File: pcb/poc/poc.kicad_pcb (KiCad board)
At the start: 2 copper layers, 100 x 100 mm, 59 parts, among them J1 USB_B_Mini, J2 Right, J3 Left, J4 AVR-ISP-6, J5 Conn_02x10_Odd_Even, J6 Conn_02x06_Odd_Even, SW1 SW_Push, SW10 SW_Push_45deg, SW11 SW_Push_45deg, SW2 SW_Push_45deg, SW3 SW_Push_45deg, SW4 SW_Push_45deg, SW5 SW_Push_45deg, SW6 SW_Push_45deg, SW7 SW_Push_45deg, SW8 SW_Push_45deg, SW9 SW_Push_45deg, U1 ATmega32U4-AU, U2 MCP23018_SO, Y1 16MHz

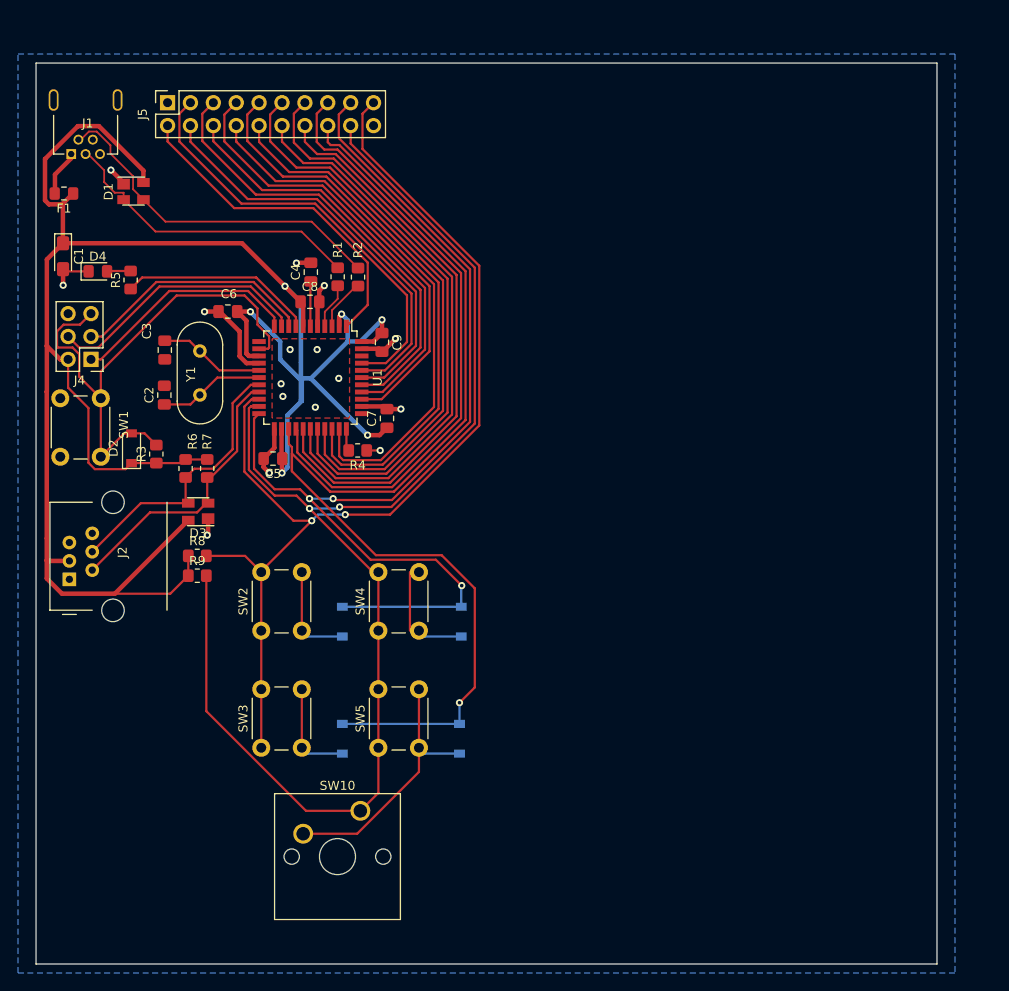
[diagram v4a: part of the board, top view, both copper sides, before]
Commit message: pcb: poc: i2c breakout and crystal ground
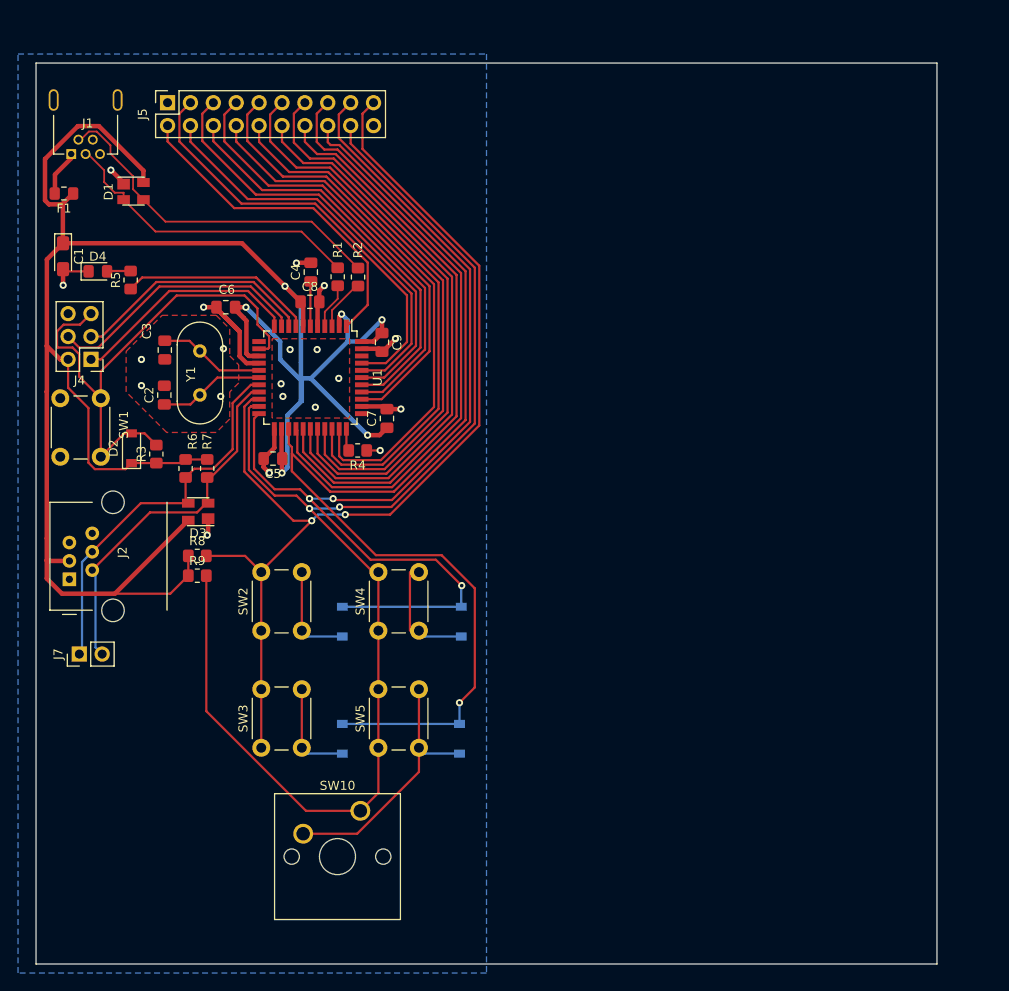
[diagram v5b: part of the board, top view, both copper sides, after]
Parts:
- added J7: Conn_01x02, Connector_PinHeader_2.54mm:PinHeader_1x02_P2.54mm_Vertical, F.Cu at (74.8, 120.6)
- moved C6 0.53 mm to (91.1, 82.1)
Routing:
- net /SCL: track 31.3 -> 43.2 mm
- net /SDA: track 31.4 -> 41.2 mm
- net GND: track 41.3 -> 45.0 mm, vias 16 -> 20
- net +5V: track 240.9 -> 243.1 mm

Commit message: pcb: poc: MCP side layout
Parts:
- added C10: 100n, Capacitor_SMD:C_0805_2012Metric_Pad1.18x1.45mm_HandSolder, F.Cu at (145.8, 75.5)
- D11, D12, D13, D14: moved to B.Cu
- moved J6 233.5 mm to (133.2, 102.5), turned to 90 degrees
- moved D14 222.5 mm to (165.0, 130.0), turned to 270 degrees
- moved SW8 214.9 mm to (156.0, 118.0), turned to 90 degrees
- moved D12 212.9 mm to (152.0, 130.0), turned to 270 degrees
- moved SW6 208.1 mm to (143.0, 118.0), turned to 90 degrees
- moved SW11 205.3 mm to (154.0, 138.0)
- moved SW9 201.1 mm to (156.0, 131.0), turned to 90 degrees
- moved U2 198.1 mm to (141.1, 67.2), turned to 90 degrees
- moved R13 197.6 mm to (135.2, 76.4), turned to 270 degrees
- moved SW7 194.5 mm to (143.0, 131.0), turned to 90 degrees
- moved R12 166.6 mm to (151.9, 63.5), turned to 90 degrees
- moved D11 160.4 mm to (152.0, 117.0), turned to 270 degrees
- moved D13 158.1 mm to (165.0, 117.0), turned to 270 degrees
- moved R10 156.3 mm to (150.5, 57.3), turned to 180 degrees
- moved R15 154.5 mm to (145.8, 59.7), turned to 180 degrees
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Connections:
- D5 pad 2: /SCL1 -> /SDA1
- D5 pad 3: /SDA1 -> /SCL1
- SW11 pad 2: Net-(D13-Pad2) -> Net-(D14-Pad2)
- U2 pad 20: /COL3 -> /COL4
- U2 pad 21: /COL4 -> /COL3
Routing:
- net /ROW3: track 0.00 -> 79.3 mm, vias 0 -> 1
- net /ROW2: track 0.00 -> 65.6 mm, vias 0 -> 1
- net +5VP: track 0.00 -> 60.9 mm
- net /COL4: track 0.00 -> 27.3 mm
- net Net-(D14-Pad2): track 0.00 -> 25.4 mm
- net /SCL1: track 0.00 -> 21.1 mm
- net /COL3: track 0.00 -> 19.5 mm
- net /SDA1: track 0.00 -> 17.3 mm
- net GND1: track 0.00 -> 6.86 mm, vias 0 -> 3
- net Net-(R10-Pad2): track 0.00 -> 6.19 mm
- net Net-(R11-Pad1): track 0.00 -> 5.58 mm
- net Net-(D13-Pad2): track 0.00 -> 4.77 mm
- net Net-(D12-Pad2): track 0.00 -> 4.77 mm
- net Net-(D11-Pad2): track 0.00 -> 4.77 mm
- net Net-(R13-Pad1): track 0.00 -> 3.63 mm
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- added copper zone on B.Cu, net GND1

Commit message: pcb: poc: Finished?
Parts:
- added J8: Conn_01x02, Connector_PinHeader_2.54mm:PinHeader_1x02_P2.54mm_Vertical, F.Cu at (162.2, 78.2)
- J6: value Conn_02x06_Odd_Even -> Conn_02x08_Odd_Even; footprint Connector_PinHeader_2.54mm:PinHeader_2x06_P2.54mm_Vertical -> Connector_PinHeader_2.54mm:PinHeader_2x08_P2.54mm_Vertical
- moved J6 4.00 mm to (133.2, 98.5)
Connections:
- J6 pad 10: /GPA6 -> /GPB4
- J6 pad 11: /GBP5 -> /GPA2
- J6 pad 12: /GPA7 -> /GPB5
- J6 pad 2: /GPA2 -> /GPA7
- J6 pad 3: /GBP1 -> /GPA6
- J6 pad 4: /GPA3 -> /GPB1
- J6 pad 5: /GBP2 -> /GPA5
- J6 pad 6: /GPA4 -> /GPB2
- J6 pad 7: /GBP3 -> /GPA4
- J6 pad 8: /GPA5 -> /GPB3
- J6 pad 9: /GBP4 -> /GPA3
- U2 pad 4: /GBP1 -> /GPB1
- U2 pad 5: /GBP2 -> /GPB2
- U2 pad 6: /GBP3 -> /GPB3
- U2 pad 7: /GBP4 -> /GPB4
- U2 pad 8: /GBP5 -> /GPB5
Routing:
- net /COL4: track 27.3 -> 161.4 mm
- net /COL3: track 19.5 -> 114.9 mm, vias 0 -> 2
- net /GPA2: track 0.00 -> 74.4 mm
- net /GPA3: track 0.00 -> 68.5 mm
- net /GPA4: track 0.00 -> 62.6 mm
- net /GPA5: track 0.00 -> 56.7 mm
- net /GPA6: track 0.00 -> 50.8 mm
- net /GPA7: track 0.00 -> 40.8 mm
- net /ROW3: track 79.3 -> 105.4 mm
- net /GPB5: track 0.00 -> 25.8 mm
- net /GPB4: track 0.00 -> 25.3 mm
- net /GPB3: track 0.00 -> 24.8 mm
- net /GPB1: track 0.00 -> 24.5 mm
- net /GPB2: track 0.00 -> 24.3 mm
- net /SDA1: track 17.3 -> 29.0 mm
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
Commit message: pcb: poc: silkscreen
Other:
- board text added: "+5"
- board text added: "A2"
- board text added: "A3"
- board text added: "A4"
- board text added: "A5"
- board text added: "A6"
- board text added: "A7"
- board text added: "B1"
- board text added: "B2"
- board text added: "B3"
- board text added: "B4"
- board text added: "B5"
- board text added: "B6"
- board text added: "C0"
- board text added: "C1"
- board text added: "C3"
- board text added: "C4"
- board text added: "C6"
- board text added: "C7"
- board text added: "D6"
- board text added: "D7"
- board text added: "E6"
- board text added: "F0"
- board text added: "F1"
- board text added: "F4"
- board text added: "F5"
- board text added: "F6"
- board text added: "F7"
- board text added: "G"
- board text added: "GND"
- board text added: "Left"
- board text added: "MISO"
- board text added: "MOSI"
- board text added: "R0"
- board text added: "R2"
- board text added: "R3"
- board text added: "RST"
- board text added: "Right"
- board text added: "SCK"
- board text added: "SCL"
- board text added: "SDA"
- board text added: "xx"
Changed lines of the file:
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@@
   (general
     (thickness 1.6)
-    (drawings 4)
+    (drawings 51)
     (tracks 686)
     (zones 0)
@@
     (pad_to_mask_clearance 0)
     (aux_axis_origin 0 0)
-    (visible_elements FFFFFFFF)
+    (visible_elements FFF7FFFF)
     (pcbplotparams
       (layerselection 0x010fc_ffffffff)
@@
     (descr "Through hole straight pin header, 2x03, 2.54mm pitch, double rows")
     (tags "Through hole pin header THT 2x03 2.54mm double row")
-    (fp_text reference J4 (at -2.4 3.89) (layer F.SilkS)
+    (fp_text reference J4 (at -2.4 3.89) (layer F.Fab)
       (effects (font (size 1 1) (thickness 0.15)))
     )
@@
     (tags "resistor handsolder")
     (attr smd)
-    (fp_text reference R11 (at 0 -1.65) (layer F.SilkS)
+    (fp_text reference R11 (at 3.5 0.4) (layer F.SilkS)
       (effects (font (size 1 1) (thickness 0.15)))
     )
@@
     (tags "QFP 0.8")
     (attr smd)
-    (fp_text reference U1 (at -1.16 -1.8 90) (layer F.SilkS)
+    (fp_text reference U1 (at 0.09 -0.15 180) (layer F.SilkS)
       (effects (font (size 1 1) (thickness 0.15)))
     )
@@
     )
   )
+  (gr_text A7 (at 133.2 93) (layer F.SilkS)
+    (effects (font (size 1 1) (thickness 0.15)))
+  )
+  (gr_text B1 (at 135.8 93) (layer F.SilkS)
+    (effects (font (size 1 1) (thickness 0.15)))
+  )
+  (gr_text B2 (at 138.2 93) (layer F.SilkS)
+    (effects (font (size 1 1) (thickness 0.15)))
+  )
+  (gr_text B3 (at 140.8 93) (layer F.SilkS)
+    (effects (font (size 1 1) (thickness 0.15)))
+  )
+  (gr_text B4 (at 143.4 93) (layer F.SilkS)
+    (effects (font (size 1 1) (thickness 0.15)))
+  )
+  (gr_text B5 (at 145.8 93) (layer F.SilkS)
+    (effects (font (size 1 1) (thickness 0.15)))
+  )
+  (gr_text C4 (at 148.4 93) (layer F.SilkS)
+    (effects (font (size 1 1) (thickness 0.15)))
+  )
+  (gr_text R2 (at 151 93) (layer F.SilkS)
+    (effects (font (size 1 1) (thickness 0.15)))
+  )
+  (gr_text R3 (at 151 101.4) (layer F.SilkS)
+    (effects (font (size 1 1) (thickness 0.15)))
+  )
+  (gr_text C3 (at 148.4 101.4) (layer F.SilkS)
+    (effects (font (size 1 1) (thickness 0.15)))
+  )
+  (gr_text A2 (at 145.8 101.4) (layer F.SilkS)
+    (effects (font (size 1 1) (thickness 0.15)))
+  )
+  (gr_text A3 (at 143.4 101.4) (layer F.SilkS)
+    (effects (font (size 1 1) (thickness 0.15)))
+  )
+  (gr_text A4 (at 140.8 101.4) (layer F.SilkS)
+    (effects (font (size 1 1) (thickness 0.15)))
+  )
+  (gr_text A5 (at 138.4 101.4) (layer F.SilkS)
+    (effects (font (size 1 1) (thickness 0.15)))
+  )
+  (gr_text A6 (at 135.8 101.4) (layer F.SilkS)
+    (effects (font (size 1 1) (thickness 0.15)))
+  )
+  (gr_text GND (at 132.8 101.4) (layer F.SilkS)
+    (effects (font (size 1 1) (thickness 0.15)))
+  )
+  (gr_text xx (at 107.6 64.6) (layer F.SilkS)
+    (effects (font (size 1 1) (thickness 0.15)))
+  )
+  (gr_text C1 (at 105 64.6) (layer F.SilkS)
+    (effects (font (size 1 1) (thickness 0.15)))
+  )
+  (gr_text R0 (at 102.4 64.6) (layer F.SilkS)
+    (effects (font (size 1 1) (thickness 0.15)))
+  )
+  (gr_text D7 (at 100 64.6) (layer F.SilkS)
+    (effects (font (size 1 1) (thickness 0.15)))
+  )
+  (gr_text B5 (at 97.4 64.6) (layer F.SilkS)
+    (effects (font (size 1 1) (thickness 0.15)))
+  )
+  (gr_text C6 (at 94.8 64.6) (layer F.SilkS)
+    (effects (font (size 1 1) (thickness 0.15)))
+  )
+  (gr_text F7 (at 92.2 64.6) (layer F.SilkS)
+    (effects (font (size 1 1) (thickness 0.15)))
+  )
+  (gr_text F5 (at 89.6 64.6) (layer F.SilkS)
+    (effects (font (size 1 1) (thickness 0.15)))
+  )
+  (gr_text F1 (at 87 64.6) (layer F.SilkS)
+    (effects (font (size 1 1) (thickness 0.15)))
+  )
+  (gr_text E6 (at 84.4 64.6) (layer F.SilkS)
+    (effects (font (size 1 1) (thickness 0.15)))
+  )
+  (gr_text C0 (at 107.6 56.8) (layer F.SilkS)
+    (effects (font (size 1 1) (thickness 0.15)))
+  )
+  (gr_text R0 (at 105 56.8) (layer F.SilkS)
+    (effects (font (size 1 1) (thickness 0.15)))
+  )
+  (gr_text D6 (at 102.4 56.8) (layer F.SilkS)
+    (effects (font (size 1 1) (thickness 0.15)))
+  )
+  (gr_text B4 (at 99.8 56.8) (layer F.SilkS)
+    (effects (font (size 1 1) (thickness 0.15)))
+  )
+  (gr_text B6 (at 97.2 56.8) (layer F.SilkS)
+    (effects (font (size 1 1) (thickness 0.15)))
+  )
+  (gr_text C7 (at 94.8 56.8) (layer F.SilkS)
+    (effects (font (size 1 1) (thickness 0.15)))
+  )
+  (gr_text F6 (at 92.2 56.8) (layer F.SilkS)
+    (effects (font (size 1 1) (thickness 0.15)))
+  )
+  (gr_text F4 (at 89.6 56.8) (layer F.SilkS)
+    (effects (font (size 1 1) (thickness 0.15)))
+  )
+  (gr_text F0 (at 87 56.8) (layer F.SilkS)
+    (effects (font (size 1 1) (thickness 0.15)))
+  )
+  (gr_text GND (at 83.8 56.8) (layer F.SilkS)
+    (effects (font (size 1 1) (thickness 0.15)))
+  )
+  (gr_text G (at 71.5 82.4) (layer F.SilkS)
+    (effects (font (size 1 1) (thickness 0.15)))
+  )
+  (gr_text +5 (at 73 90) (layer F.SilkS)
+    (effects (font (size 1 1) (thickness 0.15)))
+  )
+  (gr_text MOSI (at 71.5 85.6 90) (layer F.SilkS)
+    (effects (font (size 1 1) (thickness 0.15)))
+  )
+  (gr_text MISO (at 79.25 87.75) (layer F.SilkS)
+    (effects (font (size 1 1) (thickness 0.15)))
+  )
+  (gr_text SCK (at 79.25 85.25) (layer F.SilkS)
+    (effects (font (size 1 1) (thickness 0.15)))
+  )
+  (gr_text RST (at 79.25 82.75) (layer F.SilkS)
+    (effects (font (size 1 1) (thickness 0.15)))
+  )
+  (gr_text SDA (at 77.5 124 90) (layer F.SilkS)
+    (effects (font (size 1 1) (thickness 0.15)))
+  )
+  (gr_text SCL (at 74.75 124 90) (layer F.SilkS)
+    (effects (font (size 1 1) (thickness 0.15)))
+  )
+  (gr_text Left (at 130 149) (layer F.SilkS)
+    (effects (font (size 1 1) (thickness 0.15)))
+  )
+  (gr_text Right (at 76 149) (layer F.SilkS)
+    (effects (font (size 1 1) (thickness 0.15)))
+  )
+  (gr_line (start 122 57) (end 122 153) (layer F.SilkS) (width 0.12))
   (gr_line (start 70 155) (end 70 55) (layer Edge.Cuts) (width 0.05))
   (gr_line (start 170 155) (end 70 155) (layer Edge.Cuts) (width 0.05))
